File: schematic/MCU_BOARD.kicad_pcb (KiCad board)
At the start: 2 copper layers, 79.2 x 101.1 mm, 82 parts, among them J2 Speaker_Conn_01x02, J3 Barrel_Jack_Switch, J4 Conn_01x27, Q1 2N3904, Q2 2N3904, Q3 2N3904, Q4 2N3904, Q5 2N3904, U5 LM386, U6 74HC4051, U7 AT89S51-24PU, U9 SN74HC4060N, Y1 32.768Khz, Y2 12Mhz

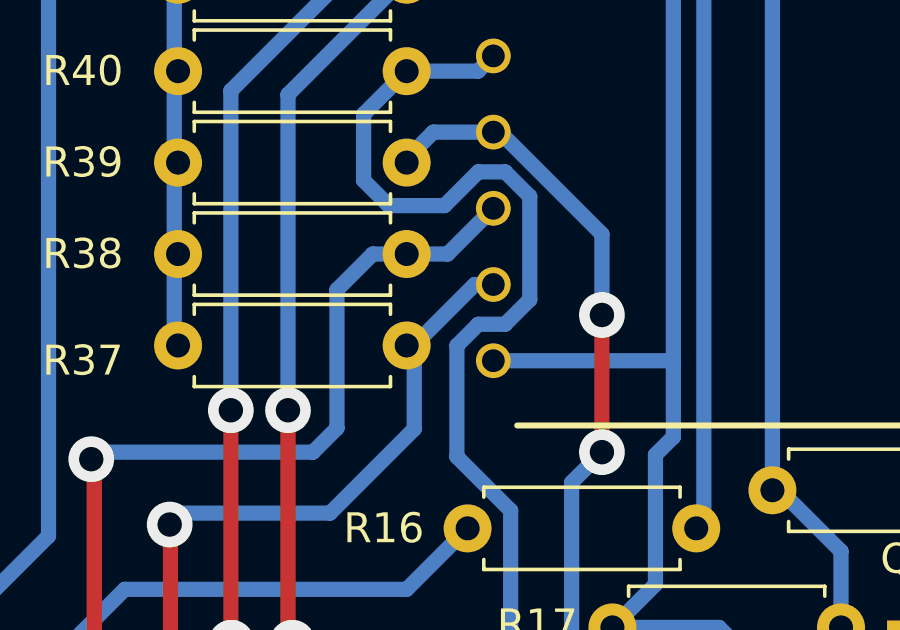
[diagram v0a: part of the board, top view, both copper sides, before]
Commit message: adjusted a trace, since ISOPRO did not pick up on it being 12 mil away.
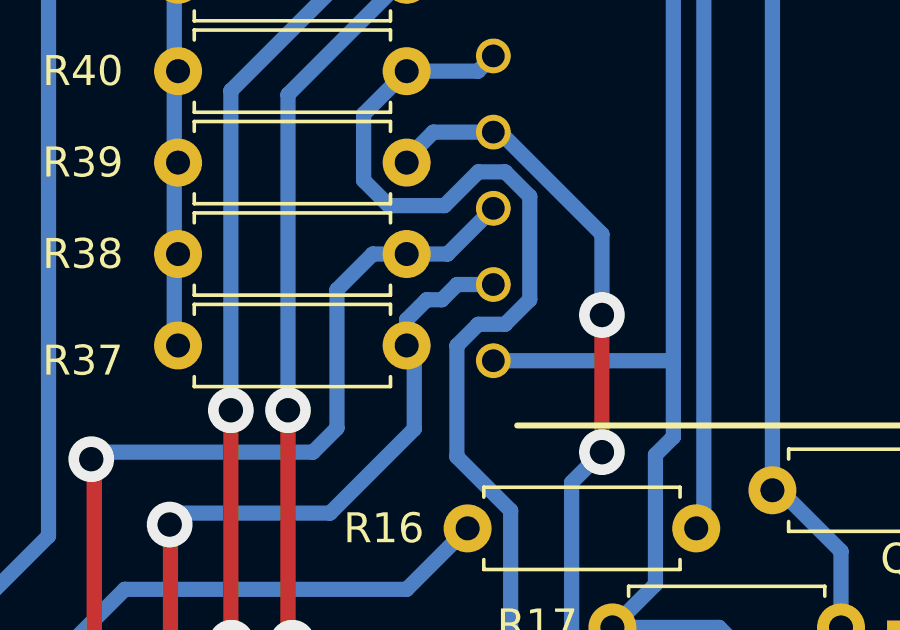
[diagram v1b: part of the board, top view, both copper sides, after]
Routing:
- net /MCU_BOARD/A: track 23.7 -> 24.9 mm
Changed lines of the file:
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@@
   (via (at 129.635 122.936) (size 1.524) (drill 0.8128) (layers "F.Cu" "B.Cu") (net 29))
   (via (at 129.609207 116.9665) (size 1.524) (drill 0.8128) (layers "F.Cu" "B.Cu") (net 29))
+  (segment (start 138.684 109.474) (end 139.192 108.966) (width 0.508) (layer "B.Cu") (net 29))
   (segment (start 129.990705 116.585002) (end 129.609207 116.9665) (width 0.508) (layer "B.Cu") (net 29))
   (segment (start 137.763 110.998) (end 137.763 113.77853) (width 0.508) (layer "B.Cu") (net 29))
   (segment (start 137.763 113.77853) (end 134.956528 116.585002) (width 0.508) (layer "B.Cu") (net 29))
-  (segment (start 140.017 108.966) (end 139.778927 108.966) (width 0.508) (layer "B.Cu") (net 29))
+  (segment (start 137.509 110.998) (end 137.509 110.141) (width 0.508) (layer "B.Cu") (net 29))
   (segment (start 137.746927 110.998) (end 137.382 110.998) (width 0.508) (layer "B.Cu") (net 29))
+  (segment (start 137.509 110.141) (end 138.176 109.474) (width 0.508) (layer "B.Cu") (net 29))
   (segment (start 134.956528 116.585002) (end 129.990705 116.585002) (width 0.508) (layer "B.Cu") (net 29))
-  (segment (start 139.778927 108.966) (end 137.746927 110.998) (width 0.508) (layer "B.Cu") (net 29))
+  (segment (start 138.176 109.474) (end 138.684 109.474) (width 0.508) (layer "B.Cu") (net 29))
   (segment (start 129.635 122.936) (end 129.635 124.968) (width 0.508) (layer "B.Cu") (net 29))
+  (segment (start 139.192 108.966) (end 140.398 108.966) (width 0.508) (layer "B.Cu") (net 29))
   (segment (start 155.956 93.726) (end 151.225 93.726) (width 0.508) (layer "B.Cu") (net 30))
   (segment (start 151.225 93.726) (end 147.415 97.536) (width 0.508) (layer "B.Cu") (net 30))

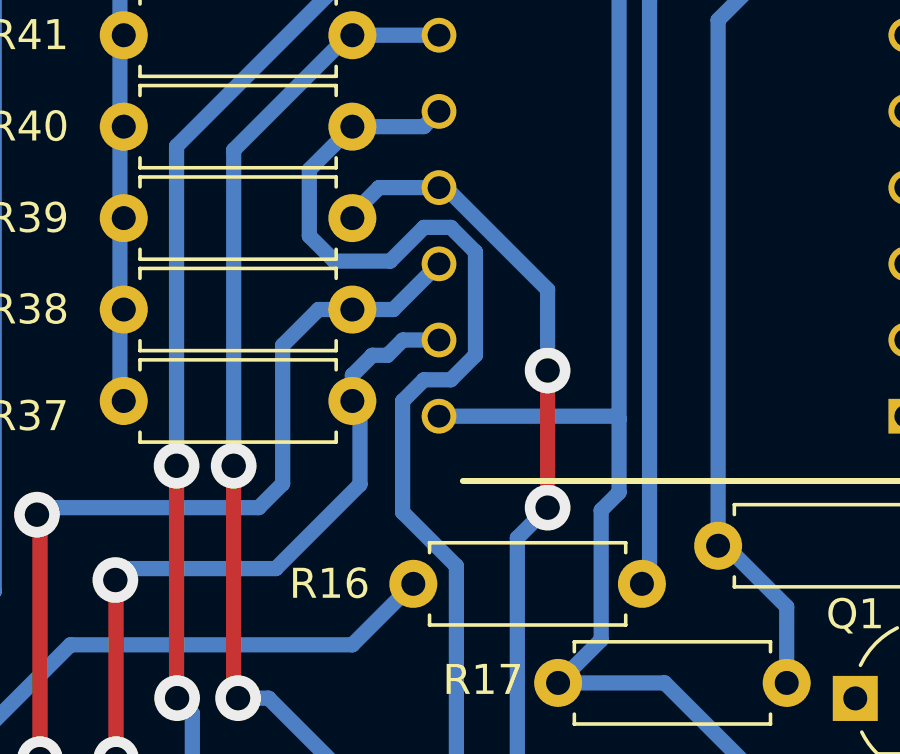
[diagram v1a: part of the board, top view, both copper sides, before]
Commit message: whoops, wrong trace, now the 12 mil trace is adjusted
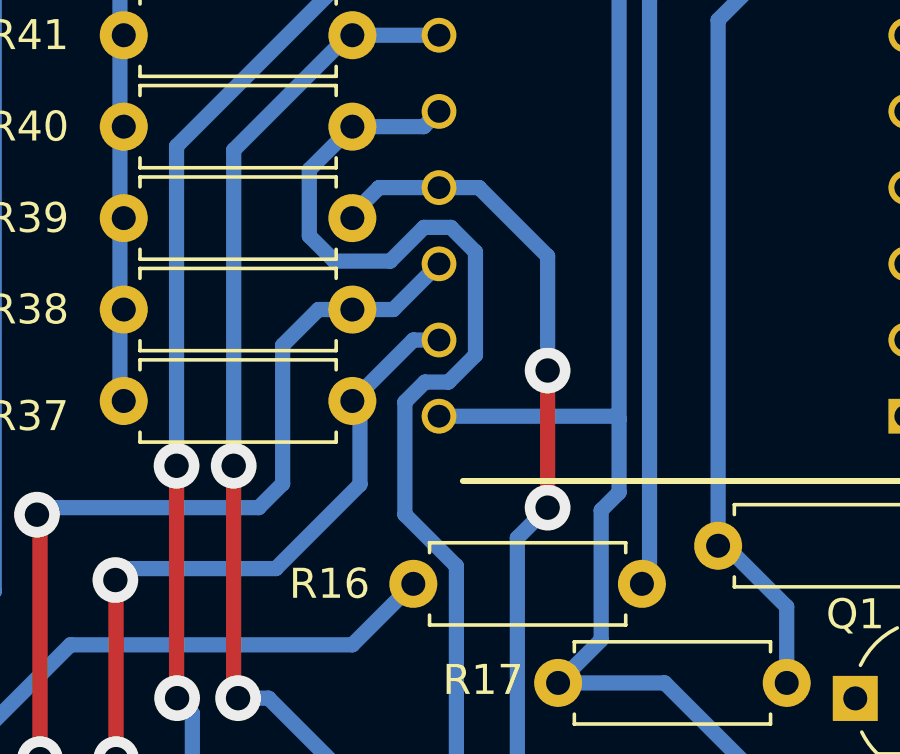
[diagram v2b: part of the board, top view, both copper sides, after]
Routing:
- net /MCU_BOARD/C: track 27.0 -> 27.6 mm
- net /MCU_BOARD/A: track 24.9 -> 24.4 mm
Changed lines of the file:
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@@
   (segment (start 137.255 123.444) (end 137.255 124.968) (width 0.508) (layer "B.Cu") (net 25))
   (segment (start 133.699 120.904) (end 134.715 120.904) (width 0.508) (layer "B.Cu") (net 25))
+  (segment (start 139.9265 110.3677) (end 139.2597 111.0345) (width 0.508) (layer "B.Cu") (net 26))
   (segment (start 136.914103 106.3365) (end 138.770644 106.3365) (width 0.508) (layer "B.Cu") (net 26))
-  (segment (start 139.1835 111.002937) (end 139.1835 114.70781) (width 0.508) (layer "B.Cu") (net 26))
+  (segment (start 138.770644 106.3365) (end 139.895644 105.2115) (width 0.508) (layer "B.Cu") (net 26))
+  (segment (start 140.713863 110.3677) (end 139.9265 110.3677) (width 0.508) (layer "B.Cu") (net 26))
+  (segment (start 139.895644 105.2115) (end 140.793299 105.2115) (width 0.508) (layer "B.Cu") (net 26))
+  (segment (start 140.976 123.787) (end 139.795 124.968) (width 0.508) (layer "B.Cu") (net 26))
+  (segment (start 137.509 101.854) (end 136.074 103.289) (width 0.508) (layer "B.Cu") (net 26))
+  (segment (start 140.976 116.50031) (end 140.976 123.787) (width 0.508) (layer "B.Cu") (net 26))
+  (segment (start 140.793299 105.2115) (end 141.6125 106.030701) (width 0.508) (layer "B.Cu") (net 26))
+  (segment (start 139.2597 111.0345) (end 139.2597 114.78401) (width 0.508) (layer "B.Cu") (net 26))
+  (segment (start 139.89 101.854) (end 140.398 101.346) (width 0.508) (layer "B.Cu") (net 26))
+  (segment (start 136.074 105.496397) (end 136.914103 106.3365) (width 0.508) (layer "B.Cu") (net 26))
+  (segment (start 141.6125 106.030701) (end 141.6125 109.469063) (width 0.508) (layer "B.Cu") (net 26))
   (segment (start 136.074 103.289) (end 136.074 105.496397) (width 0.508) (layer "B.Cu") (net 26))
-  (segment (start 139.894937 110.2915) (end 139.1835 111.002937) (width 0.508) (layer "B.Cu") (net 26))
-  (segment (start 137.509 101.854) (end 136.074 103.289) (width 0.508) (layer "B.Cu") (net 26))
-  (segment (start 136.074 105.496397) (end 136.914103 106.3365) (width 0.508) (layer "B.Cu") (net 26))
-  (segment (start 140.976 116.50031) (end 140.976 123.787) (width 0.508) (layer "B.Cu") (net 26))
-  (segment (start 139.895644 105.2115) (end 140.793299 105.2115) (width 0.508) (layer "B.Cu") (net 26))
-  (segment (start 139.89 101.854) (end 140.398 101.346) (width 0.508) (layer "B.Cu") (net 26))
-  (segment (start 140.790063 110.2915) (end 139.894937 110.2915) (width 0.508) (layer "B.Cu") (net 26))
-  (segment (start 138.770644 106.3365) (end 139.895644 105.2115) (width 0.508) (layer "B.Cu") (net 26))
-  (segment (start 140.976 123.787) (end 139.795 124.968) (width 0.508) (layer "B.Cu") (net 26))
-  (segment (start 139.1835 114.70781) (end 140.976 116.50031) (width 0.508) (layer "B.Cu") (net 26))
   (segment (start 137.509 101.854) (end 139.89 101.854) (width 0.508) (layer "B.Cu") (net 26))
-  (segment (start 141.6125 106.030701) (end 141.6125 109.469063) (width 0.508) (layer "B.Cu") (net 26))
-  (segment (start 140.793299 105.2115) (end 141.6125 106.030701) (width 0.508) (layer "B.Cu") (net 26))
-  (segment (start 141.6125 109.469063) (end 140.790063 110.2915) (width 0.508) (layer "B.Cu") (net 26))
+  (segment (start 139.2597 114.78401) (end 140.976 116.50031) (width 0.508) (layer "B.Cu") (net 26))
+  (segment (start 141.6125 109.469063) (end 140.713863 110.3677) (width 0.508) (layer "B.Cu") (net 26))
   (segment (start 144.018 109.982) (end 144.018 114.554) (width 0.508) (layer "F.Cu") (net 27))
   (via (at 144.018 114.554) (size 1.524) (drill 0.8128) (layers "F.Cu" "B.Cu") (net 27))
   (via (at 144.018 109.982) (size 1.524) (drill 0.8128) (layers "F.Cu" "B.Cu") (net 27))
   (segment (start 144.018 114.554) (end 143.0082 115.5638) (width 0.508) (layer "B.Cu") (net 27))
-  (segment (start 140.616567 103.886) (end 144.018 107.287433) (width 0.508) (layer "B.Cu") (net 27))
+  (segment (start 141.732 103.886) (end 140.398 103.886) (width 0.508) (layer "B.Cu") (net 27))
   (segment (start 138.398 103.886) (end 137.382 104.902) (width 0.508) (layer "B.Cu") (net 27))
   (segment (start 140.017 103.886) (end 138.398 103.886) (width 0.508) (layer "B.Cu") (net 27))
+  (segment (start 144.018 106.172) (end 141.732 103.886) (width 0.508) (layer "B.Cu") (net 27))
   (segment (start 143.0082 115.5638) (end 143.0082 123.1012) (width 0.508) (layer "B.Cu") (net 27))
-  (segment (start 144.018 107.287433) (end 144.018 109.982) (width 0.508) (layer "B.Cu") (net 27))
-  (segment (start 140.398 103.886) (end 140.616567 103.886) (width 0.508) (layer "B.Cu") (net 27))
+  (segment (start 144.018 109.982) (end 144.018 106.172) (width 0.508) (layer "B.Cu") (net 27))
   (segment (start 143.0082 123.1012) (end 144.875 124.968) (width 0.508) (layer "B.Cu") (net 27))
   (segment (start 127.095 122.936) (end 127.095 114.887506) (width 0.508) (layer "F.Cu") (net 28))
@@
   (via (at 129.635 122.936) (size 1.524) (drill 0.8128) (layers "F.Cu" "B.Cu") (net 29))
   (via (at 129.609207 116.9665) (size 1.524) (drill 0.8128) (layers "F.Cu" "B.Cu") (net 29))
-  (segment (start 138.684 109.474) (end 139.192 108.966) (width 0.508) (layer "B.Cu") (net 29))
+  (segment (start 137.509 110.998) (end 139.541 108.966) (width 0.508) (layer "B.Cu") (net 29))
   (segment (start 129.990705 116.585002) (end 129.609207 116.9665) (width 0.508) (layer "B.Cu") (net 29))
   (segment (start 137.763 110.998) (end 137.763 113.77853) (width 0.508) (layer "B.Cu") (net 29))
   (segment (start 137.763 113.77853) (end 134.956528 116.585002) (width 0.508) (layer "B.Cu") (net 29))
-  (segment (start 137.509 110.998) (end 137.509 110.141) (width 0.508) (layer "B.Cu") (net 29))
   (segment (start 137.746927 110.998) (end 137.382 110.998) (width 0.508) (layer "B.Cu") (net 29))
-  (segment (start 137.509 110.141) (end 138.176 109.474) (width 0.508) (layer "B.Cu") (net 29))
+  (segment (start 139.541 108.966) (end 140.398 108.966) (width 0.508) (layer "B.Cu") (net 29))
   (segment (start 134.956528 116.585002) (end 129.990705 116.585002) (width 0.508) (layer "B.Cu") (net 29))
-  (segment (start 138.176 109.474) (end 138.684 109.474) (width 0.508) (layer "B.Cu") (net 29))
   (segment (start 129.635 122.936) (end 129.635 124.968) (width 0.508) (layer "B.Cu") (net 29))
-  (segment (start 139.192 108.966) (end 140.398 108.966) (width 0.508) (layer "B.Cu") (net 29))
   (segment (start 155.956 93.726) (end 151.225 93.726) (width 0.508) (layer "B.Cu") (net 30))
   (segment (start 151.225 93.726) (end 147.415 97.536) (width 0.508) (layer "B.Cu") (net 30))

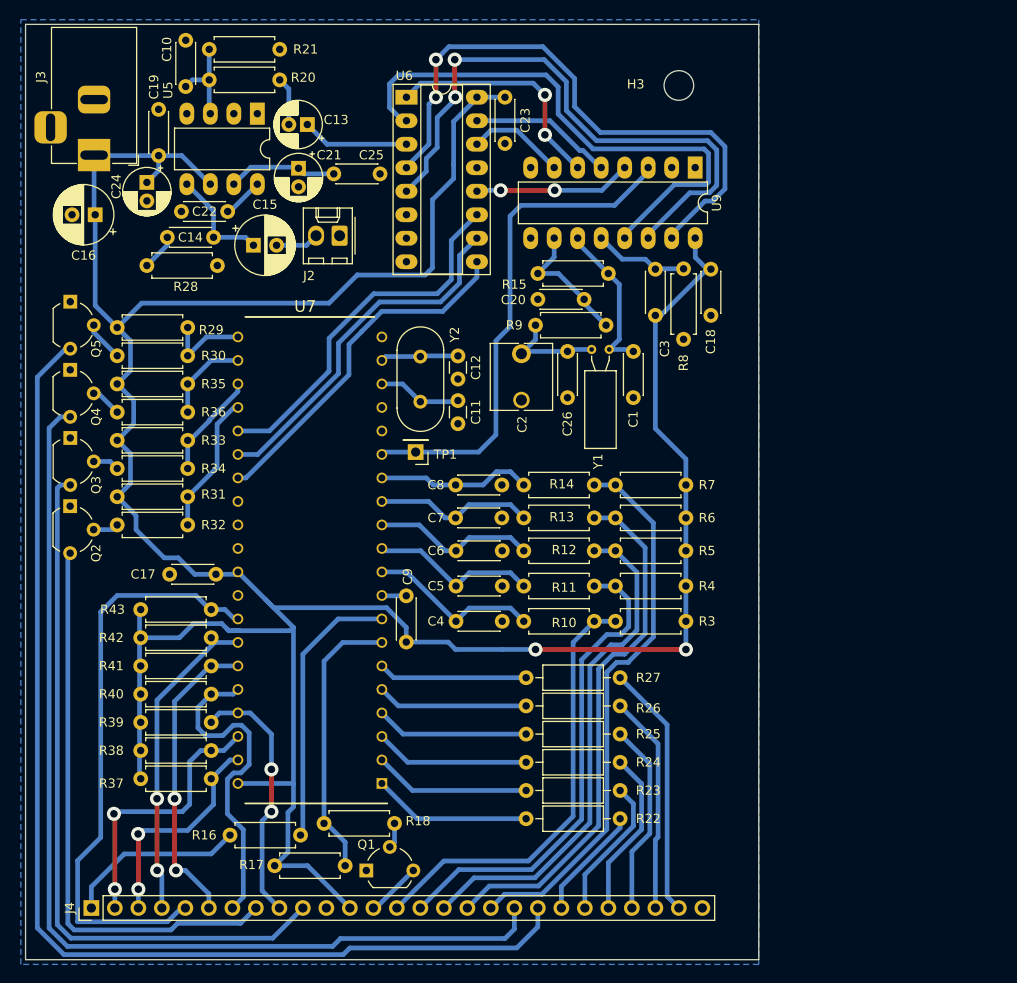
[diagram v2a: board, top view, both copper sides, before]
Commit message: added padding resistor to halve the speaker volume and deal with some noise issues in some units. Noise is originating from the 7 segment LED data lines. It runs at about 1khz so this makes sense, will try some software fixes in the future.
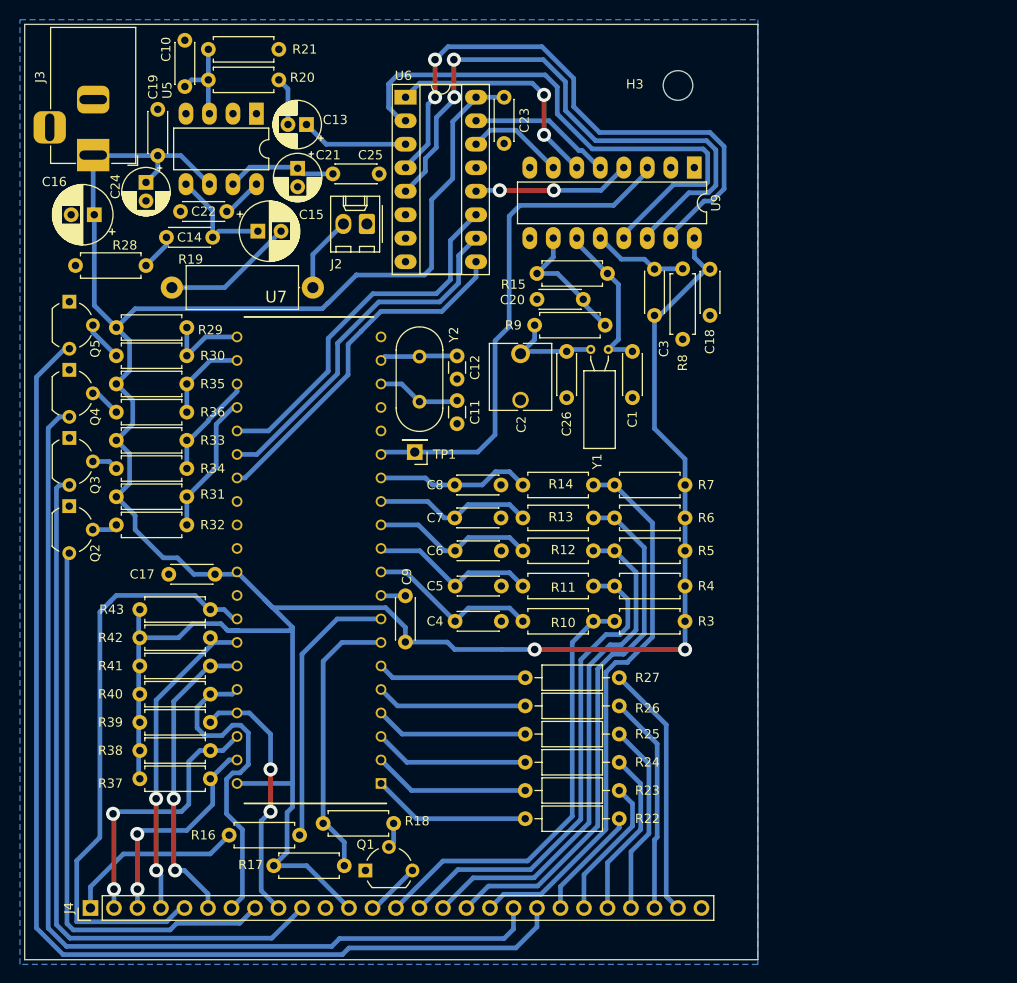
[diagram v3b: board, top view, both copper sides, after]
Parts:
- added R19: 8R_OPT, Resistor_THT:R_Axial_DIN0414_L11.9mm_D4.5mm_P15.24mm_Horizontal, F.Cu at (148.5, 57.9)
- C1: value 12pF -> 47pF
- C2: value 5-20pF -> 6-30pF
- C26: value 12pF -> 18pF
- moved J2 3.21 mm to (154.3, 51.0)
- moved C15 1.60 mm to (142.6, 51.8)
- moved J4 0.10 mm to (124.5, 125.0)
- moved C1 0.09 mm to (183.0, 69.8)
- moved C10 0.09 mm to (134.7, 36.2)
- moved C11 0.09 mm to (164.1, 72.6)
- moved C12 0.09 mm to (164.1, 65.3)
- moved C13 0.09 mm to (147.8, 40.3)
- moved C14 0.09 mm to (137.7, 52.5)
- moved C16 0.09 mm to (124.9, 50.0)
- moved C17 0.09 mm to (137.9, 88.9)
- moved C18 0.09 mm to (191.4, 55.9)
- moved C19 0.09 mm to (131.7, 43.6)
- moved C2 0.09 mm to (170.9, 70.1)
- moved C20 0.09 mm to (172.7, 59.2)
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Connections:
- C10 pad 1: (no net) -> Net-(C10-Pad1)
- C13 pad 1: (no net) -> Net-(C13-Pad1)
- C21 pad 1: (no net) -> Net-(C21-Pad1)
- C22 pad 2: (no net) -> Net-(C22-Pad2)
- C25 pad 1: (no net) -> Net-(C21-Pad1)
- J2 pad 2: Net-(C15-Pad2) -> Net-(J2-Pad2)
- R20 pad 1: (no net) -> Net-(C10-Pad1)
- R21 pad 2: (no net) -> Net-(C10-Pad1)
- U5 pad 3: (no net) -> Net-(C10-Pad1)
- U5 pad 7: (no net) -> Net-(C21-Pad1)
- U5 pad 8: (no net) -> Net-(C22-Pad2)
- U6 pad 3: (no net) -> Net-(C13-Pad1)
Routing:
- net (no net): track 37.6 -> 0.00 mm
- net Net-(C21-Pad1): track 0.00 -> 11.7 mm
- net Net-(C13-Pad1): track 0.00 -> 11.6 mm
- net Net-(C10-Pad1): track 0.00 -> 9.84 mm
- net Net-(C15-Pad2): track 4.70 -> 14.3 mm
- net Net-(J2-Pad2): track 0.00 -> 8.25 mm
- net Net-(C22-Pad2): track 0.00 -> 4.43 mm

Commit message: fixed ground issue
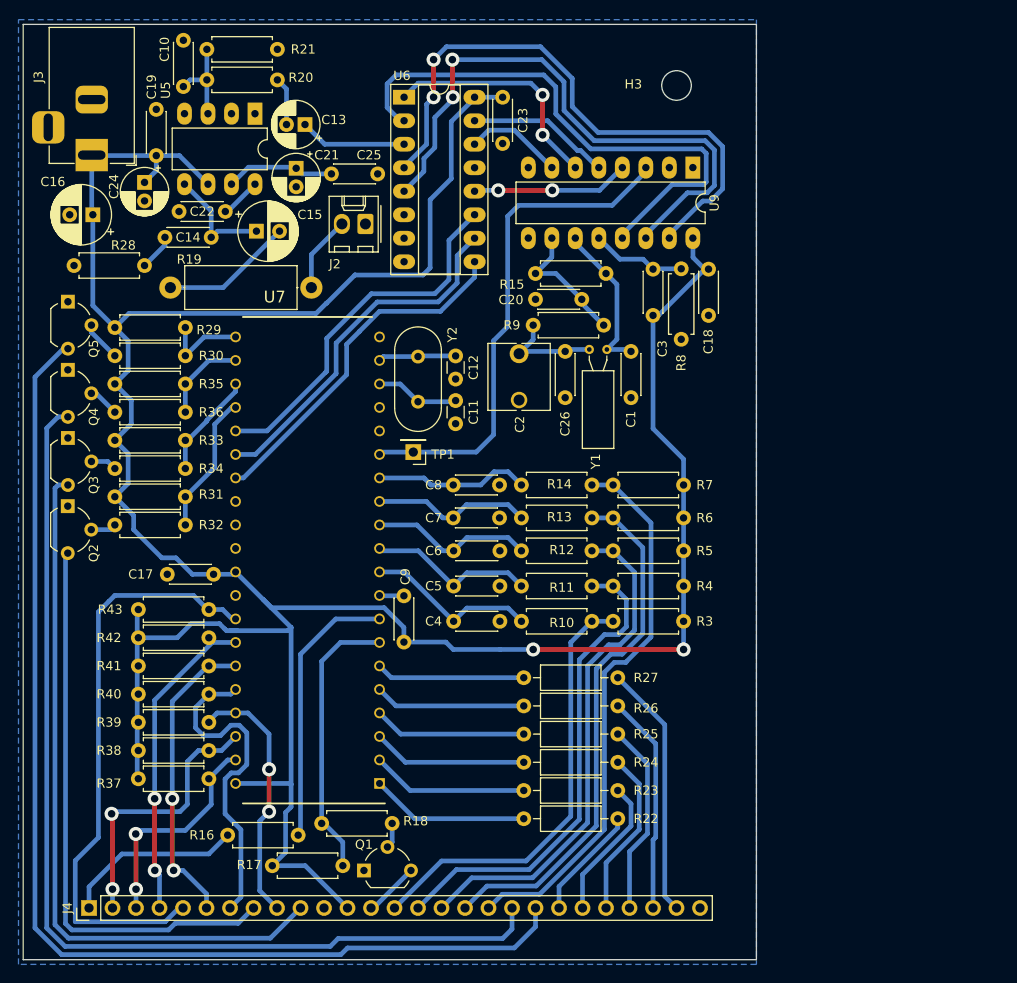
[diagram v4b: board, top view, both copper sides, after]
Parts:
- moved C10 0.16 mm to (134.5, 36.2)
- moved C2 0.16 mm to (170.8, 70.1)
- moved C24 0.16 mm to (130.3, 46.5)
- moved C7 0.16 mm to (163.7, 82.8)
- moved C8 0.16 mm to (163.7, 79.2)
- moved C9 0.16 mm to (158.3, 96.2)
- moved H3 0.16 mm to (187.8, 36.1)
- moved R22 0.16 mm to (181.5, 115.3)
- moved R23 0.16 mm to (181.5, 112.3)
- moved R24 0.16 mm to (181.5, 109.2)
- moved R25 0.16 mm to (181.5, 106.2)
- moved R26 0.16 mm to (181.5, 103.1)
- moved R27 0.16 mm to (181.5, 100.1)
- moved R28 0.16 mm to (130.3, 55.5)
- moved R9 0.16 mm to (172.3, 62.0)
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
